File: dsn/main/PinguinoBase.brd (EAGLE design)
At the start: 96.5 x 68.6 mm, 27 parts, among them IC1 7805, Q1 20MHz, X1 

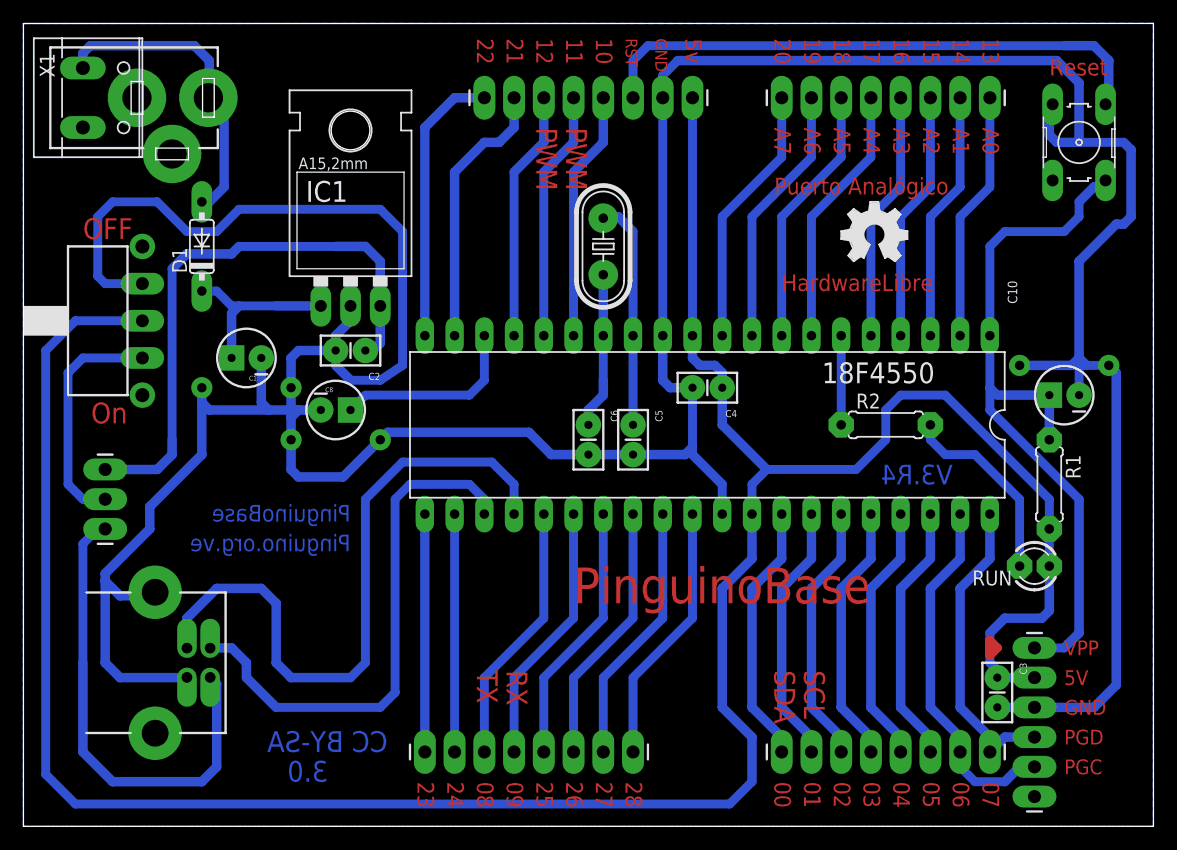
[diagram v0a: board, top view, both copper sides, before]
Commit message: Update R3.5
Nueva versión de PinguinoBase, a su versión 3.5, algunas modificaciones
de forma, reorganización de componentes, como el Cristal, capacitores,
eliminado switch de encendido, reorganizado de pistas.
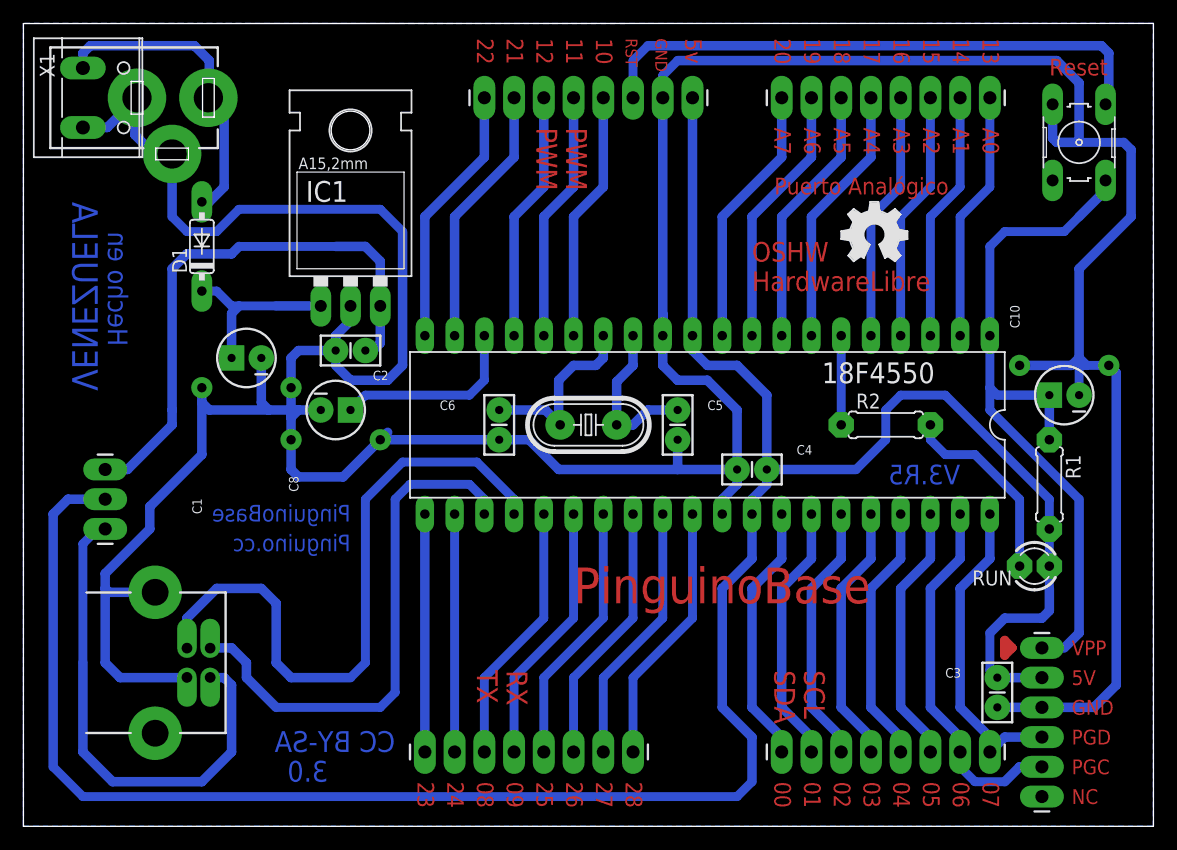
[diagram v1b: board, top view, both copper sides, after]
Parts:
- removed S1: (no value), aasanchez:TL3XYO
- moved Q1 15.3 mm to (48.3, 34.3), turned to 180 degrees
- moved C4 7.96 mm to (63.5, 30.5)
- moved C6 7.73 mm to (40.6, 35.6)
- moved C5 4.02 mm to (55.9, 35.6)
- moved JP2 0.64 mm to (87.0, 15.2)
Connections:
- removed net N$10: JP1.2, S1.1
- net +5V: now also JP1.2; no longer S1.2
- net GND: no longer S1.3
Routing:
- net N$10: track 20.1 -> 0.00 mm
- net +5V: track 226.9 -> 208.2 mm
- net GND: track 330.9 -> 341.8 mm
- net N$1: track 19.4 -> 14.1 mm
- net N$5: track 13.4 -> 15.7 mm
- net N$4: track 41.1 -> 42.8 mm
- net PIN22: track 23.9 -> 22.4 mm
- net N$3: track 49.7 -> 48.2 mm
- net N$9: track 4.97 -> 3.70 mm
- net D+: track 56.8 -> 56.1 mm
- net PIN21: track 23.2 -> 22.4 mm
- net PIN7: track 26.8 -> 27.4 mm
- net PIN6: track 31.1 -> 31.7 mm
- net RESET: track 111.4 -> 110.8 mm
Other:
- board text added: "Hecho en"
- board text added: "NC"
- board text added: "OSHW HardwareLibre"
- board text added: "Pinguino.cc"
- board text added: "V3.R5"
- board text added: "VENEZUELA"
- board text removed: "HardwareLibre"
- board text removed: "OFF"
- board text removed: "On"
- board text removed: "Pinguino.org.ve"
- board text removed: "V3.R4"

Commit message: Algunos cambios
Cambios simples en el diseño
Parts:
- removed C10: 10uf/50v, SparkFun:CPOL-RADIAL-10UF-25V
- added C7: 0.1uf, SparkFun:CAP-PTH-SMALL2
- C1: value 0.33uf/50v -> 0.1uf; device SparkFun:CPOL-RADIAL-10UF-25V -> SparkFun:CAP-PTH-SMALL2
- C3, C4: value 0.1uf -> 22pf
- C5: value 22pf -> 0.22uf/50v; device SparkFun:CAP-PTH-SMALL2 -> SparkFun:CPOL-RADIAL-10UF-25V
- C6: value 22pf -> 0.33uf/50v; device SparkFun:CAP-PTH-SMALL2 -> SparkFun:CPOL-RADIAL-10UF-25V
- C8: value 0.22uf/50v -> 10uf/50v
- JP1: device SparkFun:1X03_LONGPADS -> SparkFun:1X08_LONGPADS
- JP2: device SparkFun:1X06_LONGPADS -> SparkFun:1X08_LONGPADS
- JP3: device SparkFun:1X08_LONGPADS -> SparkFun:1X06_LONGPADS
- JP4: device SparkFun:1X08_LONGPADS -> SparkFun:1X03_LONGPADS
- R1: value 10k -> 470
- R2: value 470 -> 10k
- USB: value USB+SHIELD -> (none)
- moved JP1 84.1 mm to (82.5, 62.2), turned to 180 degrees
- moved C1 69.7 mm to (83.2, 12.7), turned to 270 degrees
- moved C8 62.2 mm to (88.9, 36.8), turned to 180 degrees
- moved JP4 62.2 mm to (6.99, 25.4), turned to 90 degrees
- moved JP2 55.7 mm to (57.1, 62.2), turned to 180 degrees
- moved JP3 47.2 mm to (87.0, 15.2), turned to 270 degrees
- moved C2 35.8 mm to (63.5, 30.5)
- moved C3 35.6 mm to (55.9, 35.6)
- moved C5 29.2 mm to (26.7, 35.6), turned to 0 degrees
- moved C4 23.4 mm to (40.6, 35.6), turned to 270 degrees
- moved C6 22.0 mm to (19.1, 40.0), turned to 180 degrees
- moved R1 14.9 mm to (73.7, 34.3), turned to 0 degrees
- moved R2 14.9 mm to (87.6, 29.2), turned to 270 degrees
- renumbered U$1 to USB
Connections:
- net +5V: now also C1.1, C2.1, JP2.1, JP3.2, JP4.2, R2.2; no longer C3.1, C4.1, JP1.2, JP2.2, JP4.1, R1.2
- net GND: now also C7.2, JP2.2, JP3.3; no longer C10.2, JP2.3, JP4.2
- net N$1: now also C3.1; no longer C5.1
- net N$2: now also C6.1; no longer C1.1
- net N$3: now also C7.1, JP4.3; no longer C2.1, JP1.3
- net N$4: now also JP4.1; no longer JP1.1
- net N$5: now also C4.1; no longer C6.1
- net N$6: now also C5.1; no longer C8.1
- net N$7: now also R1.2; no longer R2.2
- net N$8: now also R1.1; no longer R2.1
- net PIN10: now also JP2.4; no longer JP4.4
- net PIN11: now also JP2.5; no longer JP4.5
- net PIN12: now also JP2.6; no longer JP4.6
- net PIN13: now also JP1.1; no longer JP3.1
- net PIN14: now also JP1.2; no longer JP3.2
- net PIN15: now also JP1.3; no longer JP3.3
- net PIN16: now also JP1.4; no longer JP3.4
- net PIN17: now also JP1.5; no longer JP3.5
- net PIN18: now also JP1.6; no longer JP3.6
- net PIN19: now also JP1.7; no longer JP3.7
- net PIN20: now also JP1.8; no longer JP3.8
- net PIN21: now also JP2.7; no longer JP4.7
- net PIN22: now also JP2.8; no longer JP4.8
- net PIN6: now also JP3.5; no longer JP2.5
- net PIN7: now also JP3.4; no longer JP2.4
- net RESET: now also C8.1, JP2.3, JP3.1, R2.1; no longer C10.1, JP2.1, JP4.3, R1.1

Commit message: some Fixes
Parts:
- removed LOGO1: OSHW_LOGO_FILLX0200-NT, OSHW:OSHW_FILLX200_NOTEXT
- added CC_TEXT1: CREATIVE_COMMONS, SparkFun-Aesthetics:CREATIVE_COMMONS
- added LOGO2: OSHW-LOGOL, SparkFun-Aesthetics:OSHW-LOGO-L
- moved C1 1.27 mm to (84.5, 12.7)
- moved JP3 1.27 mm to (88.3, 15.2)
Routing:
- net PIN6: track 31.7 -> 33.0 mm
- net PIN7: track 27.4 -> 28.7 mm
- net RESET: track 110.8 -> 109.6 mm
- net GND: track 341.8 -> 340.5 mm
- net +5V: track 208.2 -> 208.7 mm

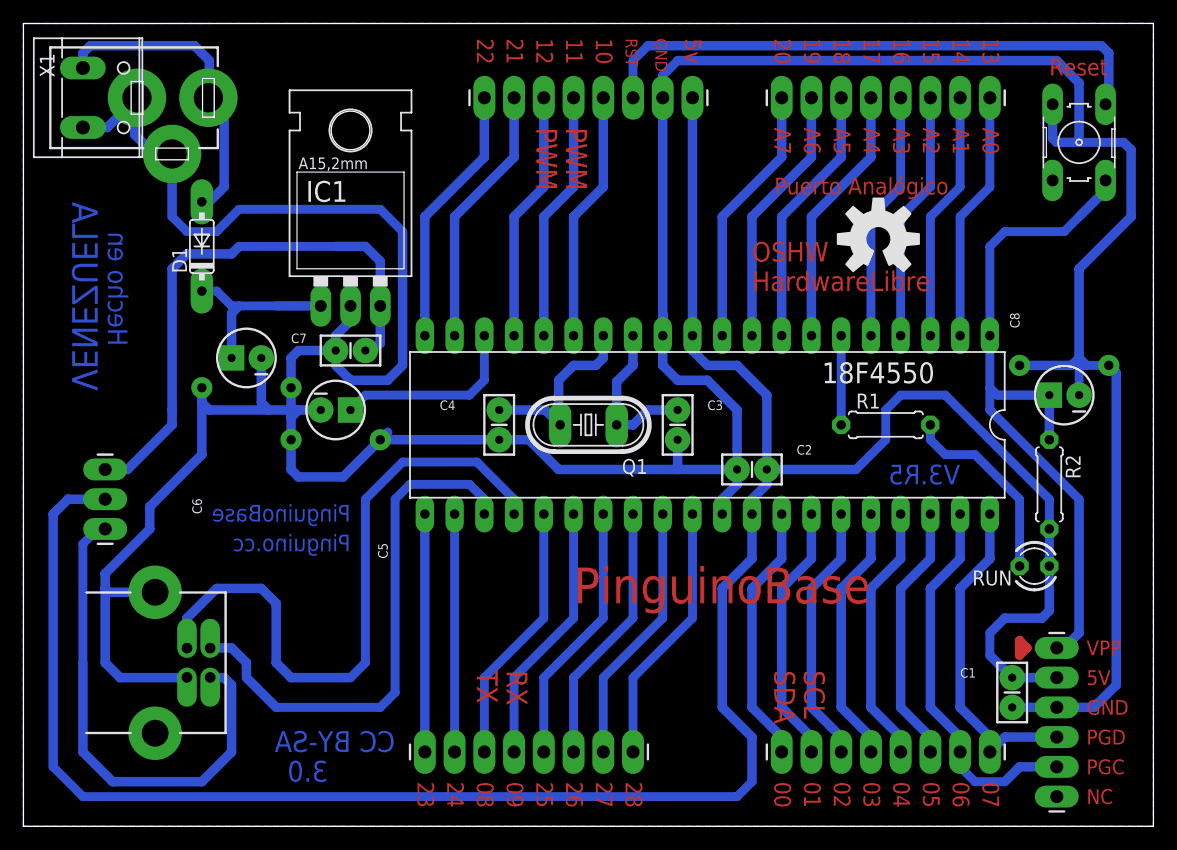
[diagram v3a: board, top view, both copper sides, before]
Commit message: Renumeracion de Componentes, mejoras en el BOM, y correccion a detalles esteticos en el Board
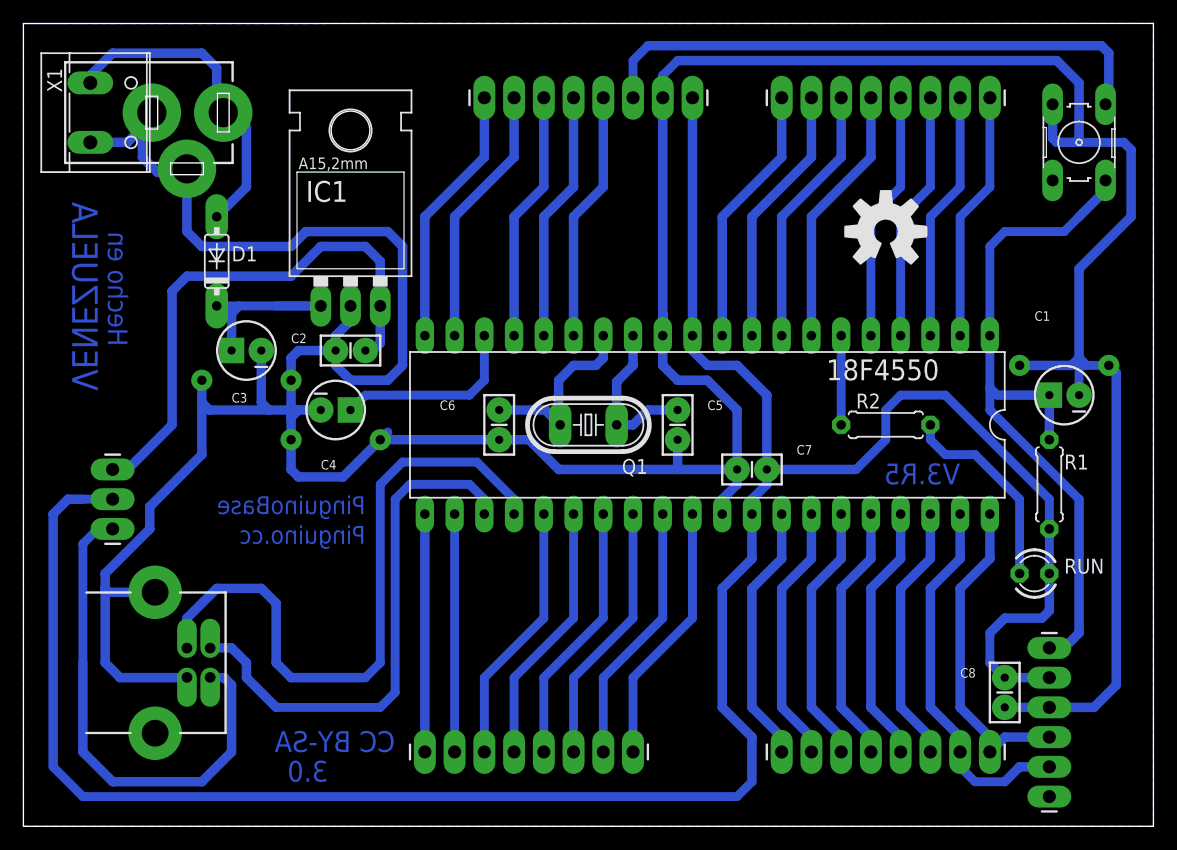
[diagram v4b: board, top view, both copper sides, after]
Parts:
- removed JP6: (no value), SparkFun:1X08_LONGPADS
- removed LOGO2: OSHW-LOGOL, SparkFun-Aesthetics:OSHW-LOGO-L
- added ICSP: (no value), SparkFun:1X06_LONGPADS
- added LOGO1: OSHW-LOGOL, SparkFun-Aesthetics:OSHW-LOGO-L
- C1: value 0.1uf -> 10uf/50v; device SparkFun:CAP-PTH-SMALL2 -> SparkFun:CPOL-RADIAL-10UF-25V
- C3: value 22pf -> 0.33uf/50v; device SparkFun:CAP-PTH-SMALL2 -> SparkFun:CPOL-RADIAL-10UF-25V
- C4: value 22pf -> 0.22uf/50v; device SparkFun:CAP-PTH-SMALL2 -> SparkFun:CPOL-RADIAL-10UF-25V
- C5: value 0.22uf/50v -> 22pf; device SparkFun:CPOL-RADIAL-10UF-25V -> SparkFun:CAP-PTH-SMALL2
- C6: value 0.33uf/50v -> 22pf; device SparkFun:CPOL-RADIAL-10UF-25V -> SparkFun:CAP-PTH-SMALL2
- C8: value 10uf/50v -> 0.1uf; device SparkFun:CPOL-RADIAL-10UF-25V -> SparkFun:CAP-PTH-SMALL2
- JP3: device SparkFun:1X06_LONGPADS -> SparkFun:1X03_LONGPADS
- JP4: device SparkFun:1X03_LONGPADS -> SparkFun:1X08_LONGPADS
- R1: value 470 -> 10k
- R2: value 10k -> 470
- moved JP4 84.1 mm to (82.5, 62.2), turned to 180 degrees
- moved JP3 81.3 mm to (7.62, 25.4), turned to 90 degrees
- moved JP2 60.4 mm to (34.3, 6.35), turned to 0 degrees
- moved JP1 58.6 mm to (64.8, 6.35), turned to 0 degrees
- moved JP5 56.4 mm to (57.1, 62.2), turned to 180 degrees
- moved C3 37.2 mm to (19.1, 40.6), turned to 180 degrees
- moved C2 35.8 mm to (29.2, 40.6)
- moved C7 35.8 mm to (63.5, 30.5)
- moved C5 29.2 mm to (55.9, 35.6), turned to 270 degrees
- moved C8 24.7 mm to (83.8, 12.7), turned to 270 degrees
- moved C1 24.5 mm to (88.9, 36.8), turned to 180 degrees
- moved C6 22.0 mm to (40.6, 35.6), turned to 270 degrees
- moved R1 14.9 mm to (87.6, 29.2), turned to 270 degrees
- moved R2 14.9 mm to (73.7, 34.3), turned to 0 degrees
- moved C4 14.0 mm to (26.7, 35.6), turned to 0 degrees
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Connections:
- net +5V: now also C7.1, C8.1, ICSP.2, JP5.1, R1.2; no longer C1.1, C2.1, JP2.1, JP4.2, R2.2
- net GND: now also ICSP.3, JP5.2; no longer JP2.2, JP3.3
- net N$1: now also C5.1; no longer C3.1
- net N$2: now also C3.1; no longer C6.1
- net N$3: now also C2.1, JP3.3; no longer C7.1, JP4.3
- net N$4: now also JP3.1; no longer JP4.1
- net N$5: now also C6.1; no longer C4.1
- net N$6: now also C4.1; no longer C5.1
- net N$7: now also R2.2; no longer R1.2
- net N$8: now also R2.1; no longer R1.1
- net PIN0: now also JP1.1; no longer JP5.1
- net PIN1: now also JP1.2; no longer JP5.2
- net PIN10: now also JP5.4; no longer JP2.4
- net PIN11: now also JP5.5; no longer JP2.5
- net PIN12: now also JP5.6; no longer JP2.6
- net PIN13: now also JP4.1; no longer JP1.1
- net PIN14: now also JP4.2; no longer JP1.2
- net PIN15: now also JP4.3; no longer JP1.3
- net PIN16: now also JP4.4; no longer JP1.4
- net PIN17: now also JP4.5; no longer JP1.5
- net PIN18: now also JP4.6; no longer JP1.6
- net PIN19: now also JP4.7; no longer JP1.7
- net PIN2: now also JP1.3; no longer JP5.3
- net PIN20: now also JP4.8; no longer JP1.8
- net PIN21: now also JP5.7; no longer JP2.7
- net PIN22: now also JP5.8; no longer JP2.8
- net PIN23: now also JP2.1; no longer JP6.1
- net PIN24: now also JP2.2; no longer JP6.2
- net PIN25: now also JP2.5; no longer JP6.5
- net PIN26: now also JP2.6; no longer JP6.6
- net PIN27: now also JP2.7; no longer JP6.7
- net PIN28: now also JP2.8; no longer JP6.8
- net PIN3: now also JP1.4; no longer JP5.4
- net PIN4: now also JP1.5; no longer JP5.5
- net PIN5: now also JP1.6; no longer JP5.6
- net PIN6: now also ICSP.5, JP1.7; no longer JP3.5, JP5.7
- net PIN7: now also ICSP.4, JP1.8; no longer JP3.4, JP5.8
- net PIN8: now also JP2.3; no longer JP6.3
- net PIN9: now also JP2.4; no longer JP6.4
- net RESET: now also C1.1, ICSP.1, JP5.3, R1.1; no longer C8.1, JP2.3, JP3.1, R2.1
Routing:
- net N$9: track 3.70 -> 0.00 mm
- net N$2: track 15.4 -> 13.0 mm
- net N$3: track 48.2 -> 46.5 mm
- net N$11: track 26.6 -> 28.0 mm
- net D+: track 56.1 -> 56.8 mm
- net PIN7: track 28.7 -> 28.0 mm
- net PIN6: track 33.0 -> 32.4 mm
- net N$4: track 42.8 -> 43.5 mm
- net N$7: track 16.7 -> 17.3 mm
- net RESET: track 109.6 -> 110.2 mm
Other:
- board text added: "+"
- board text added: "-"
- board text added: "DC-IN"
- board text added: "POWER"
- board text added: "USB"
- board text added: "VCC"
- board text added: "VSS"
- board text removed: "5V"

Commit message: Modificado posicion del Cristal
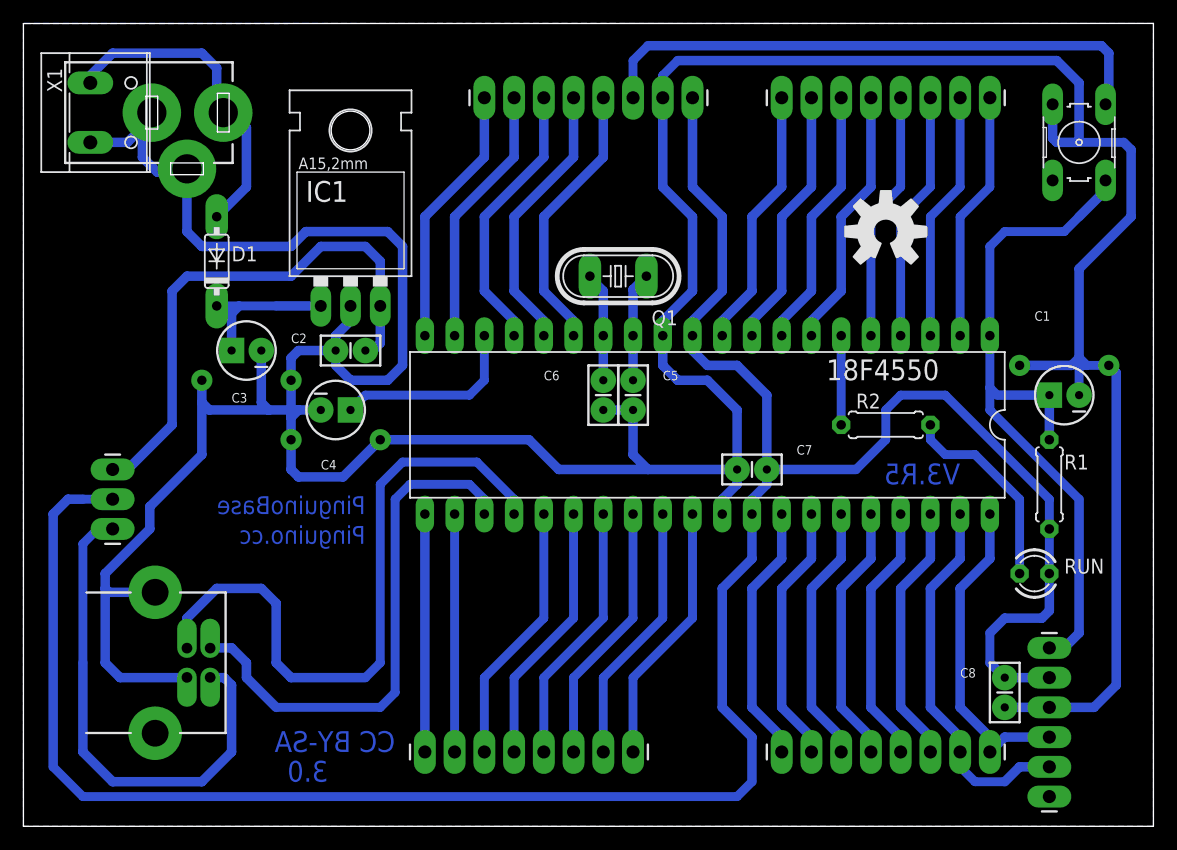
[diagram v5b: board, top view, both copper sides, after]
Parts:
- moved Q1 13.0 mm to (50.8, 47.0)
- moved C6 9.25 mm to (49.5, 38.1)
- moved C5 4.58 mm to (52.1, 38.1)
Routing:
- net N$5: track 15.7 -> 9.36 mm
- net GND: track 340.6 -> 345.5 mm
- net N$1: track 14.1 -> 9.54 mm
- net PIN11: track 21.4 -> 23.5 mm
- net PIN12: track 21.4 -> 23.5 mm
- net PIN10: track 21.4 -> 23.5 mm
- net +5V: track 209.1 -> 211.2 mm
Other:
- board text removed: "Hecho en"
- board text removed: "VENEZUELA"
